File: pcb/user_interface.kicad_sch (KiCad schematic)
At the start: 4 parts

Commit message: Add sensors sheet
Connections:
- net LED_B renamed LED0_B
- net LED_G renamed LED0_G
- net LED_R renamed LED0_R
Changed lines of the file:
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@@
 		)
 	)
-	(hierarchical_label "LED_R"
+	(hierarchical_label "LED0_R"
 		(shape input)
 		(at 38.1 50.8 270)
@@
 		)
 	)
-	(hierarchical_label "LED_G"
+	(hierarchical_label "LED0_G"
 		(shape input)
 		(at 50.8 50.8 270)
@@
 		)
 	)
-	(hierarchical_label "LED_B"
+	(hierarchical_label "LED0_B"
 		(shape input)
 		(at 63.5 50.8 270)

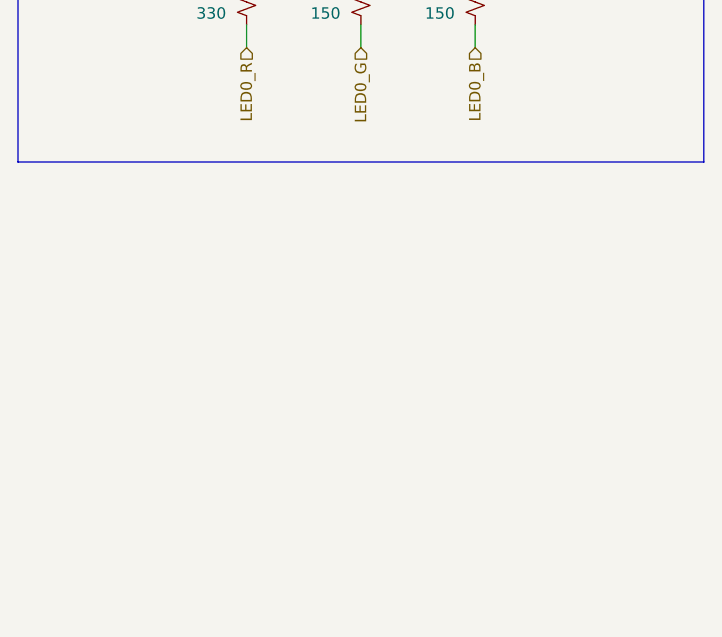
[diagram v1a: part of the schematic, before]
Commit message: Add rotary switch to user interface
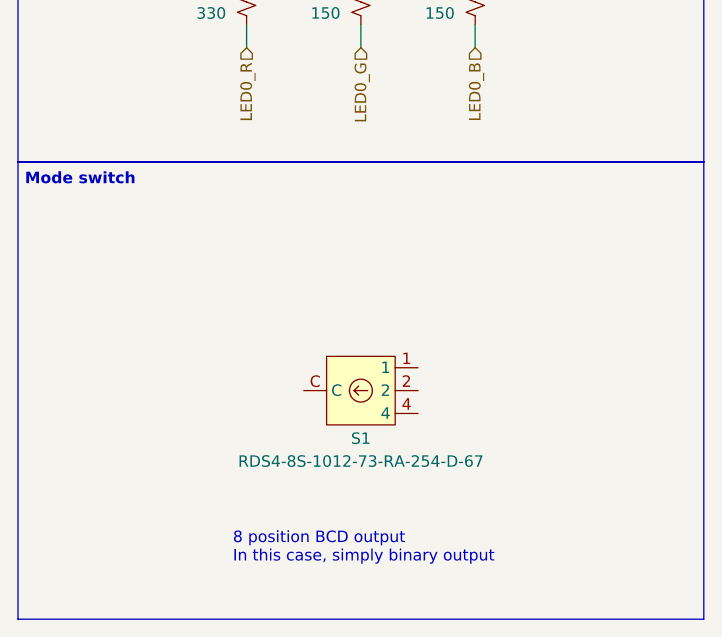
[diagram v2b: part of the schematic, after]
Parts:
- added S1: RDS4-8S-1012-73-RA-254-D-67, SW_SameSky_RDS4-8S-1012-73-RA-254-D-67:SW_RDS4-8S-1012-73-RA-254-D-67, symbol SW_SameSky_RDS4-8S-1012-73-RA-254-D-67:RDS4-8S-1012-73-RA-254-D-67
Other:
- note added: "8 position BCD output In this case, simply binary output"
- note added: "Mode switch"
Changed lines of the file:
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@@
+		)
+	)
+	(rectangle
+		(start 12.7 63.5)
+		(end 88.9 114.3)
+		(stroke
+			(width 0)
+			(type default)
+		)
+		(fill
+			(type none)
 		)
 	)
@@
 		)
 	)
+	(text "Mode switch"
+		(exclude_from_sim no)
+		(at 13.462 64.77 0)
+		(effects
+			(font
+				(size 1.27 1.27)
+				(thickness 0.254)
+				(bold yes)
+			)
+			(justify left top)
+		)
+	)
 	(text "7-8.4V"
 		(exclude_from_sim no)
@@
 				(size 1.27 1.27)
 			)
+		)
+	)
+	(text "8 position BCD output\nIn this case, simply binary output"
+		(exclude_from_sim no)
+		(at 36.576 104.648 0)
+		(effects
+			(font
+				(size 1.27 1.27)
+				(thickness 0.1588)
+			)
+			(justify left top)
 		)
 	)
@@
 					(unit 1)
 				)
+			)
+		)
+	)
+	(symbol
+		(lib_id "SW_SameSky_RDS4-8S-1012-73-RA-254-D-67:RDS4-8S-1012-73-RA-254-D-67")
+		(at 50.8 85.09 0)
+		(unit 1)
+		(exclude_from_sim no)
+		(in_bom yes)
+		(on_board yes)
+		(dnp no)
+		(property "Reference" "S1"
+			(at 50.8 94.234 0)
+			(effects
+				(font
+					(size 1.27 1.27)
+				)
+			)
+		)
+		(property "Value" "RDS4-8S-1012-73-RA-254-D-67"
+			(at 50.8 96.774 0)
+			(effects
+				(font
+					(size 1.27 1.27)
+				)
+			)
+		)
+		(property "Footprint" "SW_SameSky_RDS4-8S-1012-73-RA-254-D-67:SW_RDS4-8S-1012-73-RA-254-D-67"
+			(at 50.8 80.01 0)
+			(effects
+				(font
+					(size 1.27 1.27)
+				)
+				(justify bottom)
+				(hide yes)
+			)
+		)
+		(property "Datasheet" "https://www.sameskydevices.com/product/resource/rds4-1012-ra-67.pdf"
+			(at 49.53 79.248 0)
+			(effects
+				(font
+					(size 1.27 1.27)
+				)
+				(hide yes)
+			)
+		)
+		(property "Description" "8 Position, Through Hole, 2.54 mm Pitch, IP67, Right Angle, 7.3 mm Raised Actuator, DIP Switch"
+			(at 49.53 79.248 0)
+			(effects
+				(font
+					(size 1.27 1.27)
+				)
+				(hide yes)
+			)
+		)
+		(pin "NC"
+		)
+		(pin "2"
+		)
+		(pin "C"
+		)
+		(pin "1"
+		)
+		(pin "4"
+		)
+		(instances
+			(project ""
+				(path "/1f4fd4ed-9886-4375-a5ac-dc32d5760936/0a32b07f-7988-40ae-8006-b298a5ae2a50"
+					(reference "S1")
+					(unit 1)
+				)

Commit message: Add buzzer symbol to user interface
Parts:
- added BZ1: CEM-1203(42), Buzzer_SameSky:Buzzer_SameSky_CEM-1203_42, symbol Device:Buzzer
- added D4: SS12, symbol Device:D_Schottky_Small
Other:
- note added: "BAT54 good tho allegedly"
- note added: "Buzzer"
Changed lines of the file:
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@@
+	)
+	(rectangle
+		(start 12.7 114.3)
+		(end 88.9 165.1)
+		(stroke
+			(width 0)
+			(type default)
+		)
+		(fill
+			(type none)
+		)
 	)
 	(rectangle
@@
 		)
 	)
+	(text "Buzzer"
+		(exclude_from_sim no)
+		(at 13.716 116.078 0)
+		(effects
+			(font
+				(size 1.27 1.27)
+				(thickness 0.254)
+				(bold yes)
+			)
+			(justify left top)
+		)
+	)
 	(text "red 2V\ngreen/blue 3V"
 		(exclude_from_sim no)
 		(at 79.248 33.782 0)
+		(effects
+			(font
+				(size 1.27 1.27)
+			)
+		)
+	)
+	(text "BAT54 good\ntho allegedly"
+		(exclude_from_sim no)
+		(at 21.844 133.604 0)
 		(effects
 			(font
@@
 			)
 			(justify right)
+		)
+	)
+	(symbol
+		(lib_id "Device:Buzzer")
+		(at 53.34 133.35 0)
+		(unit 1)
+		(exclude_from_sim no)
+		(in_bom yes)
+		(on_board yes)
+		(dnp no)
+		(fields_autoplaced yes)
+		(property "Reference" "BZ1"
+			(at 57.15 132.0799 0)
+			(effects
+				(font
+					(size 1.27 1.27)
+				)
+				(justify left)
+			)
+		)
+		(property "Value" "CEM-1203(42)"
+			(at 57.15 134.6199 0)
+			(effects
+				(font
+					(size 1.27 1.27)
+				)
+				(justify left)
+			)
+		)
+		(property "Footprint" "Buzzer_SameSky:Buzzer_SameSky_CEM-1203_42"
+			(at 52.705 130.81 90)
+			(effects
+				(font
+					(size 1.27 1.27)
+				)
+				(hide yes)
+			)
+		)
+		(property "Datasheet" "~"
+			(at 52.705 130.81 90)
+			(effects
+				(font
+					(size 1.27 1.27)
+				)
+				(hide yes)
+			)
+		)
+		(property "Description" "Buzzer, polarized"
+			(at 53.34 133.35 0)
+			(effects
+				(font
+					(size 1.27 1.27)
+				)
+				(hide yes)
+			)
+		)
+		(pin "1"
+		)
+		(pin "2"
+		)
+		(instances
+			(project ""
+				(path "/1f4fd4ed-9886-4375-a5ac-dc32d5760936/0a32b07f-7988-40ae-8006-b298a5ae2a50"
+					(reference "BZ1")
+					(unit 1)
+				)
+			)
 		)
 	)
@@
 					(unit 1)
 				)
+			)
+		)
+	)
+	(symbol
+		(lib_id "Device:D_Schottky_Small")
+		(at 31.75 133.35 270)
+		(unit 1)
+		(exclude_from_sim no)
+		(in_bom yes)
+		(on_board yes)
+		(dnp no)
+		(fields_autoplaced yes)
+		(property "Reference" "D4"
+			(at 34.29 131.8259 90)
+			(effects
+				(font
+					(size 1.27 1.27)
+				)
+				(justify left)
+			)
+		)
+		(property "Value" "SS12"
+			(at 34.29 134.3659 90)
+			(effects
+				(font
+					(size 1.27 1.27)
+				)
+				(justify left)
+			)
+		)
+		(property "Footprint" ""
+			(at 31.75 133.35 90)
+			(effects
+				(font
+					(size 1.27 1.27)
+				)
+				(hide yes)
+			)
+		)
+		(property "Datasheet" "~"
+			(at 31.75 133.35 90)
+			(effects
+				(font
+					(size 1.27 1.27)
+				)
+				(hide yes)
+			)
+		)
+		(property "Description" "Schottky diode, small symbol"
+			(at 31.75 133.35 0)
+			(effects
+				(font
+					(size 1.27 1.27)
+				)
+				(hide yes)
+			)
+		)
+		(pin "2"
+		)
+		(pin "1"
+		)
+		(instances
+			(project ""
+				(path "/1f4fd4ed-9886-4375-a5ac-dc32d5760936/0a32b07f-7988-40ae-8006-b298a5ae2a50"
+					(reference "D4")
+					(unit 1)
+				)
+			)
+		)
+	)
+	(symbol
+		(lib_id "power:+3V3")
+		(at 46.99 123.19 0)
+		(unit 1)
+		(exclude_from_sim no)
+		(in_bom yes)
+		(on_board yes)
+		(dnp no)
+		(fields_autoplaced yes)
+		(property "Reference" "#PWR069"
+			(at 46.99 127 0)
+			(effects
+				(font
+					(size 1.27 1.27)
+				)
+				(hide yes)
+			)
+		)
+		(property "Value" "+3V3"
+			(at 46.99 118.11 0)
+			(effects
+				(font
+					(size 1.27 1.27)
+				)
+			)
+		)
+		(property "Footprint" ""
+			(at 46.99 123.19 0)
+			(effects
+				(font
+					(size 1.27 1.27)
+				)
+				(hide yes)
+			)
+		)
+		(property "Datasheet" ""
+			(at 46.99 123.19 0)
+			(effects
+				(font
+					(size 1.27 1.27)
+				)
+				(hide yes)
+			)
+		)
+		(property "Description" "Power symbol creates a global label with name \"+3V3\""
+			(at 46.99 123.19 0)
+			(effects
+				(font
+					(size 1.27 1.27)
+				)
+				(hide yes)
+			)
+		)
+		(pin "1"
+		)
+		(instances
+			(project ""
+				(path "/1f4fd4ed-9886-4375-a5ac-dc32d5760936/0a32b07f-7988-40ae-8006-b298a5ae2a50"
+					(reference "#PWR069")
+					(unit 1)
+				)

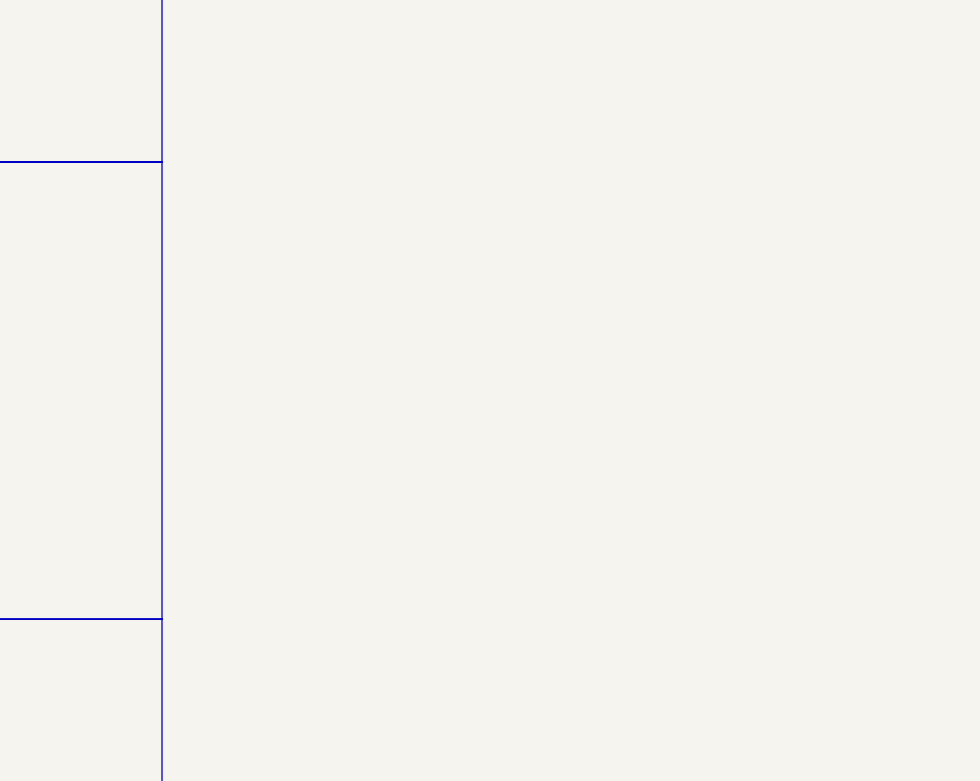
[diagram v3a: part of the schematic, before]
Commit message: Add buzzer and move servo
Buzzer - TIM16 CH1 PB8
Servo - TIM17 CH1 PB9
SERVO_EN PE0
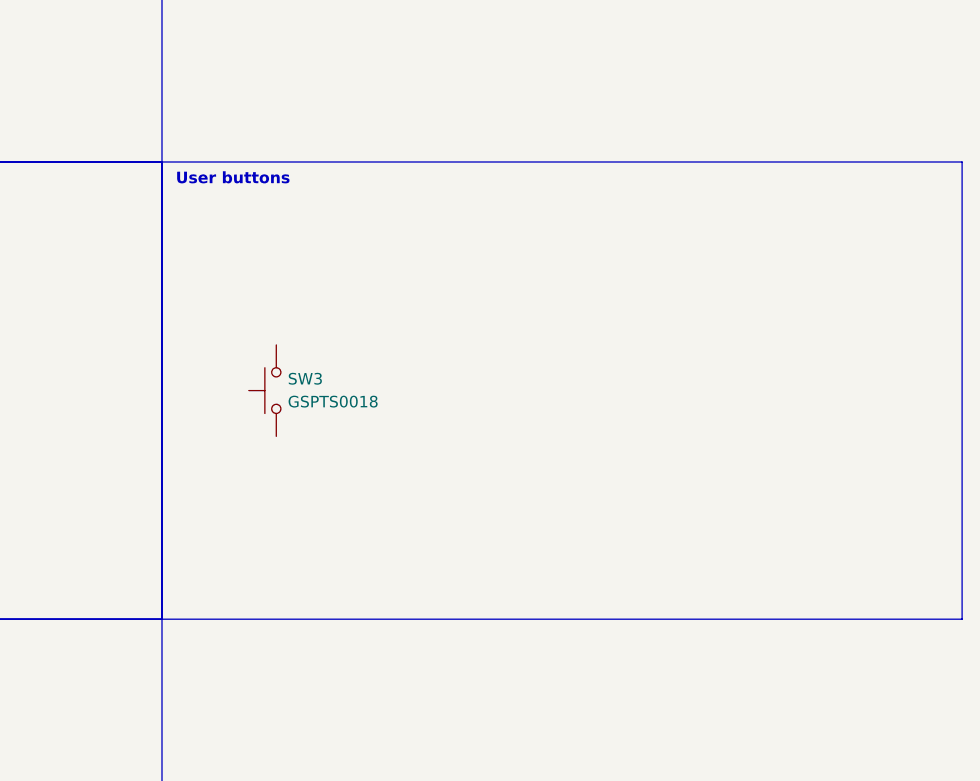
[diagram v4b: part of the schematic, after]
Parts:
- added SW3: GSPTS0018, PTS815_SJM_250_SMTR_LFS:SW_Push_PTS815_SJM_250_SMTR_LFS, symbol Switch:SW_Push
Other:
- note added: "User buttons"
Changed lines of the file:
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@@
 	(paper "A4")
+	(rectangle
+		(start 88.9 63.5)
+		(end 177.8 114.3)
+		(stroke
+			(width 0)
+			(type default)
+		)
+		(fill
+			(type none)
+		)
+	)
 	(rectangle
 		(start 12.7 12.7)
@@
 				(size 1.27 1.27)
 			)
+		)
+	)
+	(text "User buttons"
+		(exclude_from_sim no)
+		(at 90.424 64.77 0)
+		(effects
+			(font
+				(size 1.27 1.27)
+				(thickness 0.254)
+				(bold yes)
+			)
+			(justify left top)
 		)
 	)
@@
 					(unit 1)
 				)
+			)
+		)
+	)
+	(symbol
+		(lib_id "Switch:SW_Push")
+		(at 101.6 88.9 90)
+		(unit 1)
+		(exclude_from_sim no)
+		(in_bom yes)
+		(on_board yes)
+		(dnp no)
+		(fields_autoplaced yes)
+		(property "Reference" "SW3"
+			(at 102.87 87.6299 90)
+			(effects
+				(font
+					(size 1.27 1.27)
+				)
+				(justify right)
+			)
+		)
+		(property "Value" "GSPTS0018"
+			(at 102.87 90.1699 90)
+			(effects
+				(font
+					(size 1.27 1.27)
+				)
+				(justify right)
+			)
+		)
+		(property "Footprint" "PTS815_SJM_250_SMTR_LFS:SW_Push_PTS815_SJM_250_SMTR_LFS"
+			(at 96.52 88.9 0)
+			(effects
+				(font
+					(size 1.27 1.27)
+				)
+				(hide yes)
+			)
+		)
+		(property "Datasheet" "https://www.ckswitches.com/media/2728/pts815.pdf"
+			(at 96.52 88.9 0)
+			(effects
+				(font
+					(size 1.27 1.27)
+				)
+				(hide yes)
+			)
+		)
+		(property "Description" "Push button switch, generic, two pins"
+			(at 101.6 88.9 0)
+			(effects
+				(font
+					(size 1.27 1.27)
+				)
+				(hide yes)
+			)
+		)
+		(pin "2"
+		)
+		(pin "1"
+		)
+		(instances
+			(project ""
+				(path "/1f4fd4ed-9886-4375-a5ac-dc32d5760936/0a32b07f-7988-40ae-8006-b298a5ae2a50"
+					(reference "SW3")
+					(unit 1)
+				)
